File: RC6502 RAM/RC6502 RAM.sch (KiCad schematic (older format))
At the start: 9 parts, among them J1 Page PullUp, J2 Bus enable, J3 CONN_01X39, U1 HM62256BLP-7, U2 74HCT00

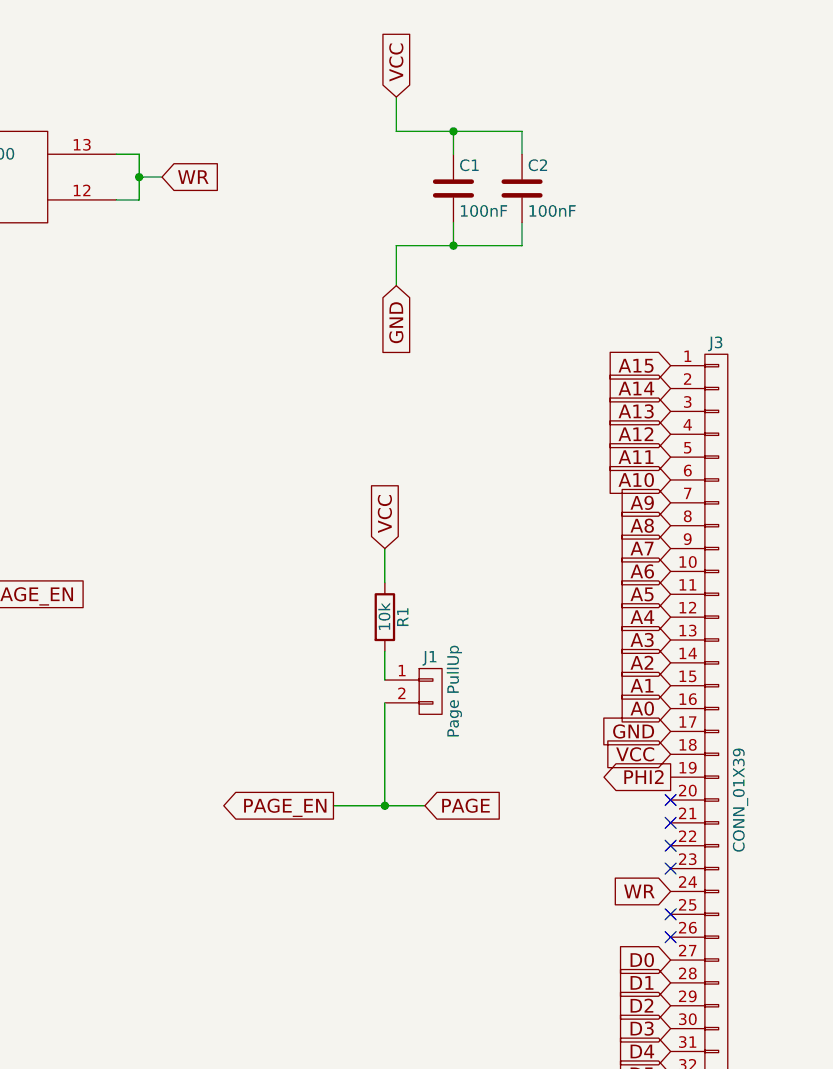
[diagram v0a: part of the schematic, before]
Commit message: Renamed some pins
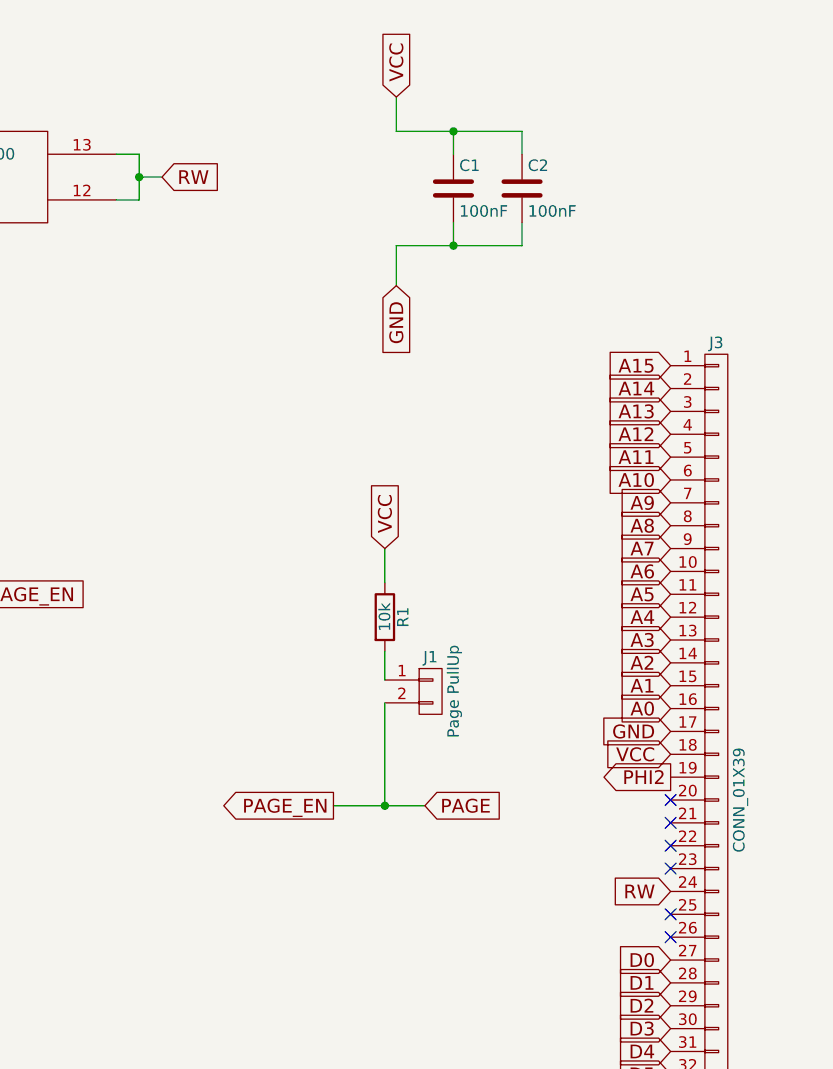
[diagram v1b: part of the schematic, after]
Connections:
- net WR renamed RW
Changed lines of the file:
@@
 $EndComp
 Text GLabel 9100 4450 0    60   Input ~ 0
-WR
+RW
 Text GLabel 9100 3750 0    60   Input ~ 0
 GND
@@
 NoConn ~ 9100 5550
 NoConn ~ 9100 5650
-Text GLabel 7850 2950 1    60   Input ~ 0
-VCC
-Text GLabel 7625 4075 0    60   Output ~ 0
-PAGE_EN
 Text GLabel 8425 5850 0    60   Output ~ 0
 PAGE
-Text GLabel 8025 4075 2    60   Input ~ 0
-PAGE
-$Comp
-L R R1
-U 1 1 590BED30
-P 7850 3250
-F 0 "R1" V 7930 3250 50  0000 C CNN
-F 1 "10k" V 7850 3250 50  0000 C CNN
-F 2 "Resistors_THT:R_Axial_DIN0207_L6.3mm_D2.5mm_P10.16mm_Horizontal" V 7780 3250 50  0001 C CNN
-F 3 "" H 7850 3250 50  0001 C CNN
-	1    7850 3250
-	1    0    0    -1
-$EndComp
-$Comp
-L CONN_01X02 J1
-U 1 1 590C6113
-P 8050 3575
-F 0 "J1" H 8050 3725 50  0000 C CNN
-F 1 "Page PullUp" V 8150 3575 50  0000 C CNN
-F 2 "Pin_Headers:Pin_Header_Angled_1x02_Pitch2.54mm" H 8050 3575 50  0001 C CNN
-F 3 "" H 8050 3575 50  0001 C CNN
-	1    8050 3575
-	1    0    0    -1
-$EndComp
 Text GLabel 1450 2425 0    60   Input ~ 0
 A14
@@
 $EndComp
 Text GLabel 6875 1325 2    60   Input ~ 0
-WR
+RW
 $Comp
 L 74HCT00 U2
@@
 Wire Wire Line
 	8675 5850 9100 5850
-Wire Wire Line
-	7625 4075 8025 4075
-Wire Wire Line
-	7850 3625 7850 4075
-Connection ~ 7850 4075
-Wire Wire Line
-	7850 3525 7850 3400
-Wire Wire Line
-	7850 3100 7850 2950
 Wire Wire Line
 	2450 1975 3100 1975
@@
 Wire Wire Line
 	8450 1625 8450 1525
+Wire Wire Line
+	7850 3100 7850 2950
+Wire Wire Line
+	7850 3525 7850 3400
+Connection ~ 7850 4075
+Wire Wire Line
+	7850 3625 7850 4075
+Wire Wire Line
+	7625 4075 8025 4075
+$Comp
+L CONN_01X02 J1
+U 1 1 590C6113
+P 8050 3575
+F 0 "J1" H 8050 3725 50  0000 C CNN
+F 1 "Page PullUp" V 8150 3575 50  0000 C CNN
+F 2 "Pin_Headers:Pin_Header_Angled_1x02_Pitch2.54mm" H 8050 3575 50  0001 C CNN
+F 3 "" H 8050 3575 50  0001 C CNN
+	1    8050 3575
+	1    0    0    -1
+$EndComp
+$Comp
+L R R1
+U 1 1 590BED30
+P 7850 3250
+F 0 "R1" V 7930 3250 50  0000 C CNN
+F 1 "10k" V 7850 3250 50  0000 C CNN
+F 2 "Resistors_THT:R_Axial_DIN0207_L6.3mm_D2.5mm_P10.16mm_Horizontal" V 7780 3250 50  0001 C CNN
+F 3 "" H 7850 3250 50  0001 C CNN
+	1    7850 3250
+	1    0    0    -1
+$EndComp
+Text GLabel 8025 4075 2    60   Input ~ 0
+PAGE
+Text GLabel 7625 4075 0    60   Output ~ 0
+PAGE_EN
+Text GLabel 7850 2950 1    60   Input ~ 0
+VCC
 $EndSCHEMATC

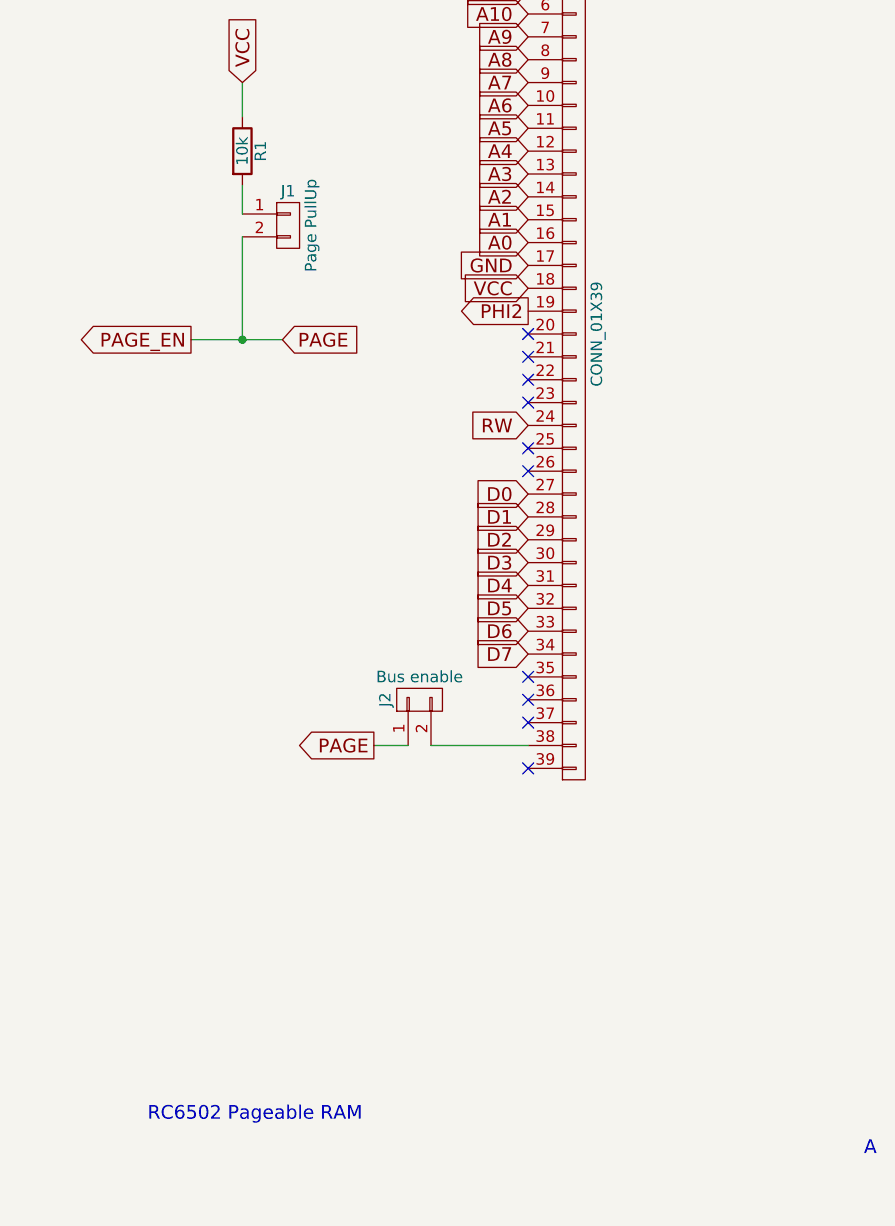
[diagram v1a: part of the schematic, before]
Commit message: RAM revision B
Fixed silkscreen notes by swapping high/low text, moved around tracks to make it a little more compact.
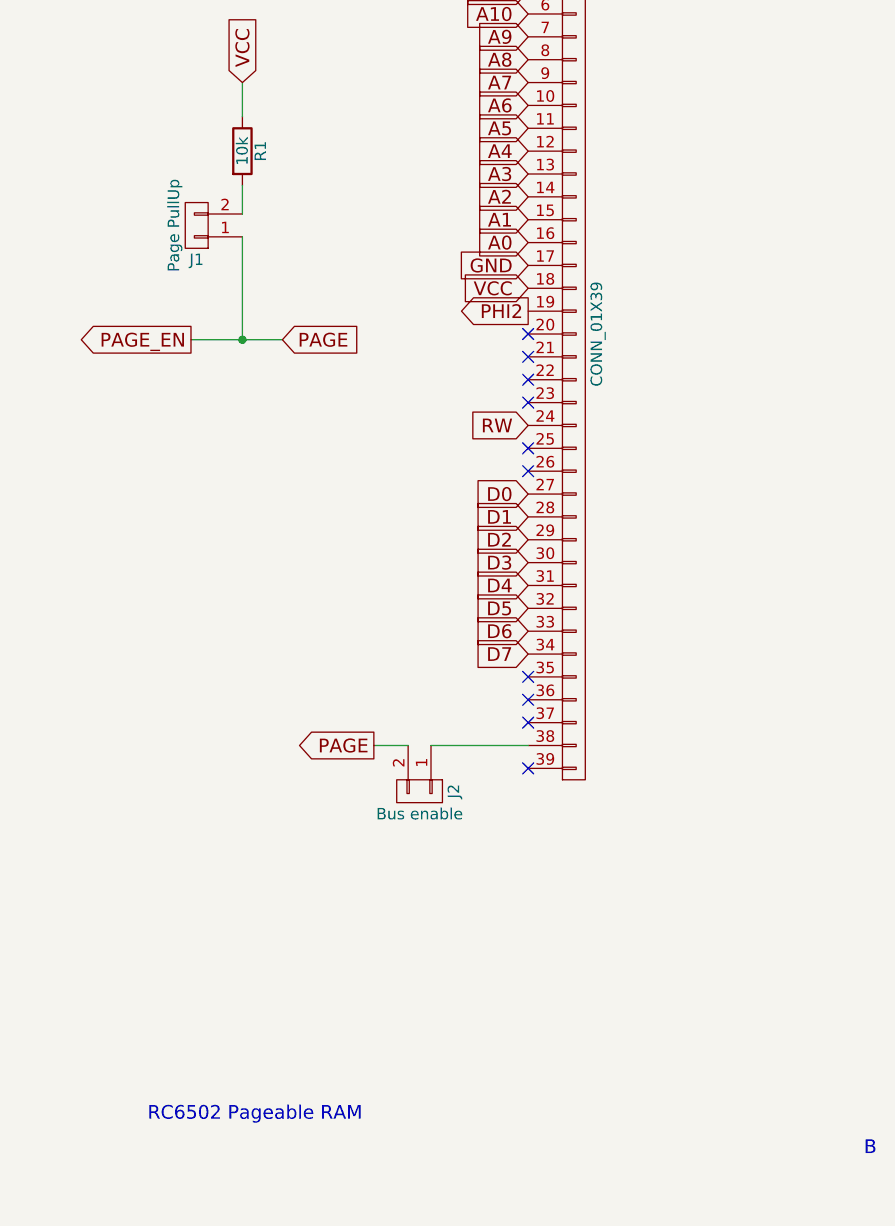
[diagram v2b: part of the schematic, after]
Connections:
- net PAGE: now also J1.1 (P1), J2.2 (P2); no longer J1.2 (P2), J2.1 (P1)
- net at J3.38 (P38): now also J2.1 (P1); no longer J2.2 (P2)
- net at R1.2: now also J1.2 (P2); no longer J1.1 (P1)
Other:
- note added: "B"
- note removed: "A"
- moved on the sheet: J1, J2
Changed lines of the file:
@@
 RC6502 Pageable RAM
 Text Notes 10625 7650 2    60   ~ 0
-A
+B
 NoConn ~ -500 7850
 $Comp
@@
 L CONN_01X02 J2
 U 1 1 590B8522
-P 8625 5650
-F 0 "J2" H 8625 5800 50  0000 C CNN
-F 1 "Bus enable" V 8725 5650 50  0000 C CNN
-F 2 "Pin_Headers:Pin_Header_Angled_1x02_Pitch2.54mm" H 8625 5650 50  0001 C CNN
-F 3 "" H 8625 5650 50  0001 C CNN
-	1    8625 5650
-	0    -1   -1   0
+P 8625 6050
+F 0 "J2" H 8625 6200 50  0000 C CNN
+F 1 "Bus enable" V 8725 6050 50  0000 C CNN
+F 2 "Pin_Headers:Pin_Header_Angled_1x02_Pitch2.54mm" H 8625 6050 50  0001 C CNN
+F 3 "" H 8625 6050 50  0001 C CNN
+	1    8625 6050
+	0    1    1    0
 $EndComp
 NoConn ~ 9100 5950
@@
 L CONN_01X02 J1
 U 1 1 590C6113
-P 8050 3575
-F 0 "J1" H 8050 3725 50  0000 C CNN
-F 1 "Page PullUp" V 8150 3575 50  0000 C CNN
-F 2 "Pin_Headers:Pin_Header_Angled_1x02_Pitch2.54mm" H 8050 3575 50  0001 C CNN
-F 3 "" H 8050 3575 50  0001 C CNN
-	1    8050 3575
-	1    0    0    -1
-$EndComp
-$Comp
+P 7650 3575
+F 0 "J1" H 7650 3725 50  0000 C CNN
+F 1 "Page PullUp" V 7750 3575 50  0000 C CNN
+F 2 "Pin_Headers:Pin_Header_Angled_1x02_Pitch2.54mm" H 7650 3575 50  0001 C CNN
+F 3 "" H 7650 3575 50  0001 C CNN
+	1    7650 3575
+	-1   0    0    1
+$EndComp
+$Comp

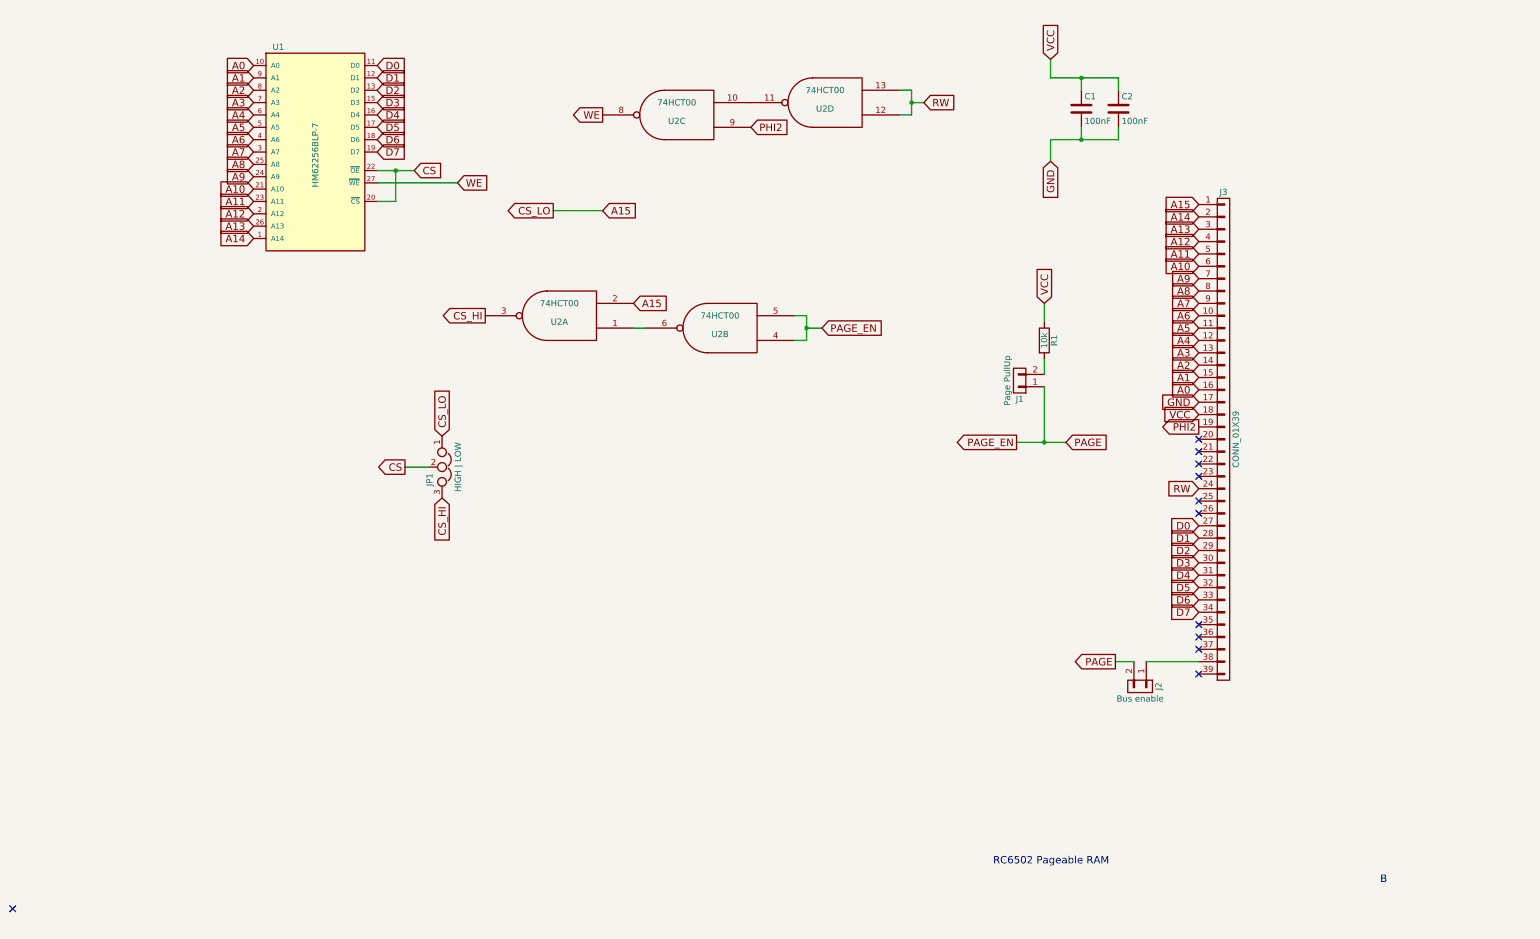
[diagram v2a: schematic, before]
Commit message: Schematic done for enhanced RAM/ROM board
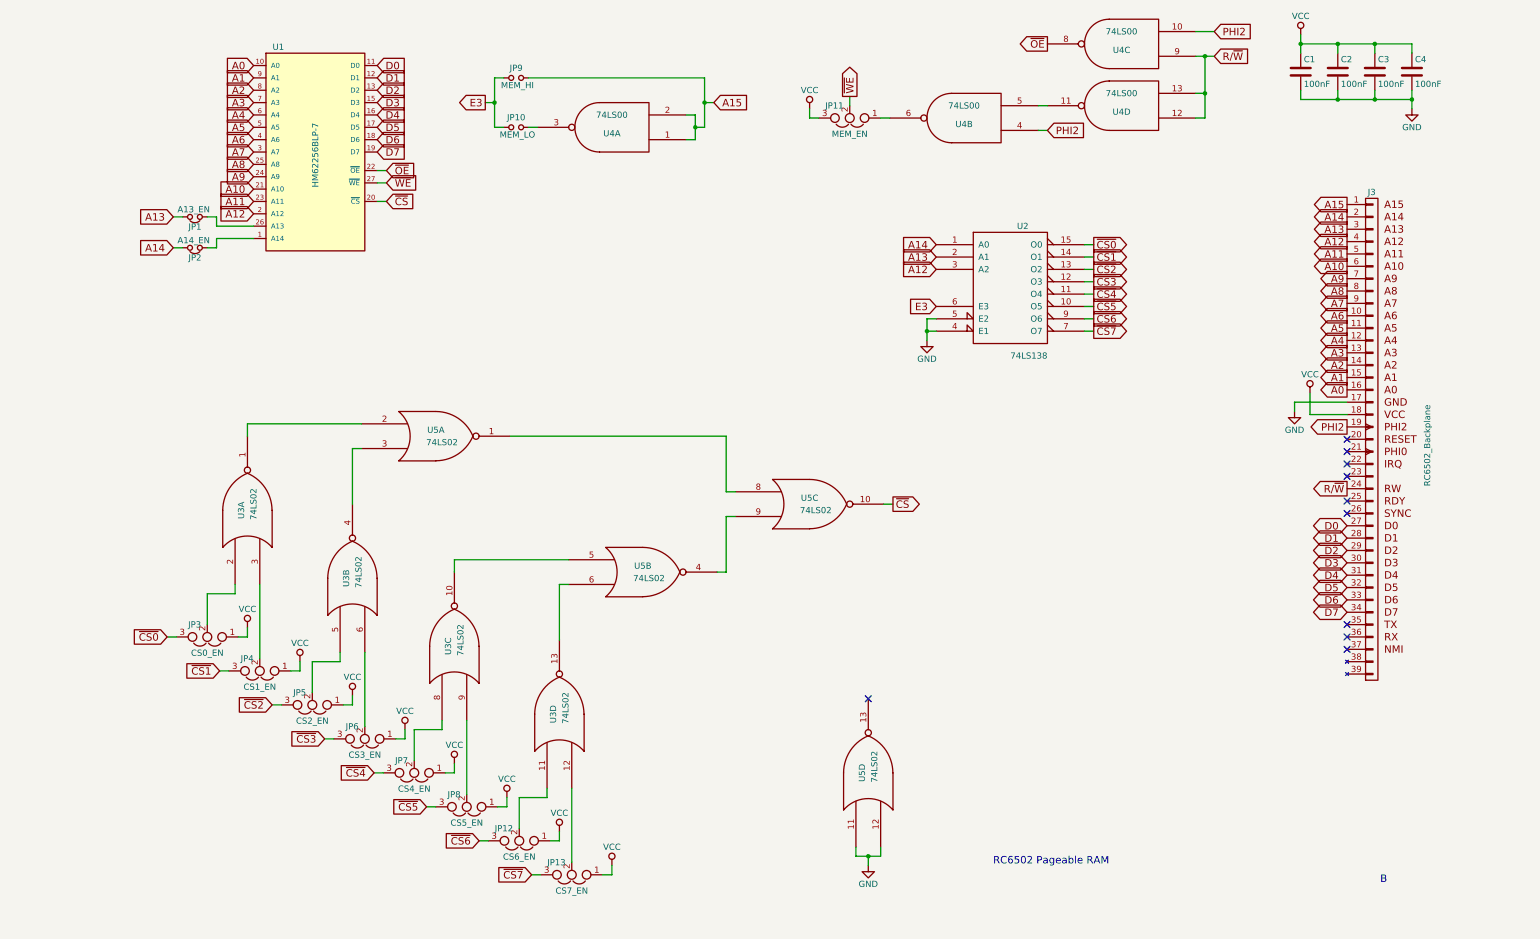
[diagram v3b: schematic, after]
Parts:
- removed J1: Page PullUp, Pin_Headers:Pin_Header_Angled_1x02_Pitch2.54mm, symbol CONN_01X02
- removed J2: Bus enable, Pin_Headers:Pin_Header_Angled_1x02_Pitch2.54mm, symbol CONN_01X02
- removed J3: CONN_01X39, Pin_Headers:Pin_Header_Angled_1x39_Pitch2.54mm, symbol CONN_01X39
- removed JP1: HIGH | LOW, Pin_Headers:Pin_Header_Angled_1x03_Pitch2.54mm, symbol Jumper_NC_Dual
- removed R1: 10k, Resistors_THT:R_Axial_DIN0207_L6.3mm_D2.5mm_P10.16mm_Horizontal, symbol R
- removed U2: 74HCT00, Housings_DIP:DIP-14_W7.62mm_Socket, symbol 74HCT00
- added C1, C4: 100nF, Capacitors_THT:C_Disc_D4.7mm_W2.5mm_P5.00mm, symbol C
- added J3: RC6502_Backplane, symbol RC6502_Backplane
- added JP1: A13_EN, symbol Jumper_NC_Small
- added JP10: MEM_LO, symbol Jumper_NO_Small
- added JP11: MEM_EN, symbol Jumper_NC_Dual
- added JP12: CS6_EN, symbol Jumper_NC_Dual
- added JP13: CS7_EN, symbol Jumper_NC_Dual
- added JP2: A14_EN, symbol Jumper_NC_Small
- added JP3: CS0_EN, symbol Jumper_NC_Dual
- added JP4: CS1_EN, symbol Jumper_NC_Dual
- added JP5: CS2_EN, symbol Jumper_NC_Dual
- added JP6: CS3_EN, symbol Jumper_NC_Dual
- added JP7: CS4_EN, symbol Jumper_NC_Dual
- added JP8: CS5_EN, symbol Jumper_NC_Dual
- added JP9: MEM_HI, symbol Jumper_NO_Small
- added U2: 74LS138, symbol 74LS138
- added U3, U5: 74LS02, symbol 74LS02
- added U4: 74LS00, symbol 74LS00
- renumbered C1 to C2, C2 to C3
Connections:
- net A0: now also J3.16 (A0)
- net A1: now also J3.15 (A1)
- net A10: now also J3.6 (A10)
- net A11: now also J3.5 (A11)
- net A12: now also J3.4 (A12), U2.3 (A2)
- net A13: now also J3.3 (A13), JP1.2, U2.2 (A1); no longer U1.26 (A13)
- net A14: now also J3.2 (A14), JP2.2, U2.1 (A0); no longer U1.1 (A14)
- net A15: now also J3.1 (A15), JP9.2, U4.1, U4.2
- net A2: now also J3.14 (A2)
- net A3: now also J3.13 (A3)
- net A4: now also J3.12 (A4)
- net A5: now also J3.11 (A5)
- net A6: now also J3.10 (A6)
- net A7: now also J3.9 (A7)
- net A8: now also J3.8 (A8)
- net A9: now also J3.7 (A9)
- net D0: now also J3.27 (D0)
- net D1: now also J3.28 (D1)
- net D2: now also J3.29 (D2)
- net D3: now also J3.30 (D3)
- net D4: now also J3.31 (D4)
- net D5: now also J3.32 (D5)
- net D6: now also J3.33 (D6)
- net D7: now also J3.34 (D7)
- net GND: now also C1.2, C4.2, J3.17 (P17), U2.4 (E1), U2.5 (E2), U2.8 (GND), U3.7 (GND), U3.7 (GND), U3.7 (GND), U3.7 (GND), U4.7 (GND), U4.7 (GND), U4.7 (GND), U4.7 (GND), U5.11, U5.12, U5.7 (GND), U5.7 (GND), U5.7 (GND), U5.7 (GND)
- net PHI2: now also J3.19 (PHI2), U4.10, U4.4
- net VCC: now also C1.1, C4.1, J3.18 (P18), JP11.3, JP12.1, JP13.1, JP3.1, JP4.1, JP5.1, JP6.1, JP7.1, JP8.1, U2.16 (VCC), U3.14 (VCC), U3.14 (VCC), U3.14 (VCC), U3.14 (VCC), U4.14 (VCC), U4.14 (VCC), U4.14 (VCC), U4.14 (VCC), U5.14 (VCC), U5.14 (VCC), U5.14 (VCC), U5.14 (VCC)
- net CS renamed ~CS
- net ~CS: now also U5.10; no longer U1.22 (~OE)
- net WE renamed ~WE
- net ~WE: now also JP11.2
- new net: JP2.1, U1.1 (A14)
- new net: JP1.1, U1.26 (A13)
- new net: JP10.2, U4.3
- new net: U4.11, U4.5
- new net: JP11.1, U4.6
- new net: JP3.2, U3.2
- new net: U3.1, U5.2
- new net: JP4.2, U3.3
- new net: JP5.2, U3.5
- new net: U3.4, U5.3
- new net: JP6.2, U3.6
- new net: JP7.2, U3.8
- new net: U3.10, U5.5
- new net: JP8.2, U3.9
- new net: JP12.2, U3.11
- new net: JP13.2, U3.12
- new net: U3.13, U5.6
- new net: U5.1, U5.8
- new net: U5.4, U5.9
- new net E3: JP10.1, JP9.1, U2.6 (E3)
- new net R/~W: J3.24 (RW), U4.12, U4.13, U4.9
- new net ~CS0: JP3.3, U2.15 (O0)
- new net ~CS1: JP4.3, U2.14 (O1)
- new net ~CS2: JP5.3, U2.13 (O2)
- new net ~CS3: JP6.3, U2.12 (O3)
- new net ~CS4: JP7.3, U2.11 (O4)
- new net ~CS5: JP8.3, U2.10 (O5)
- new net ~CS6: JP12.3, U2.9 (O6)
- new net ~CS7: JP13.3, U2.7 (O7)
- new net ~OE: U1.22 (~OE), U4.8
- no-connect marks 11 -> 10
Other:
- moved on the sheet: C2, C3
